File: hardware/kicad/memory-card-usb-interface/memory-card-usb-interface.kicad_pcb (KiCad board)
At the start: 2 copper layers, 16.6 x 40 mm, 9 parts, among them J1 USB_B, J2 DB9_Male, J3 CONN_MCU_VPP, J4 CONN_MCU_LOG, U1 PIC16F1454-IP

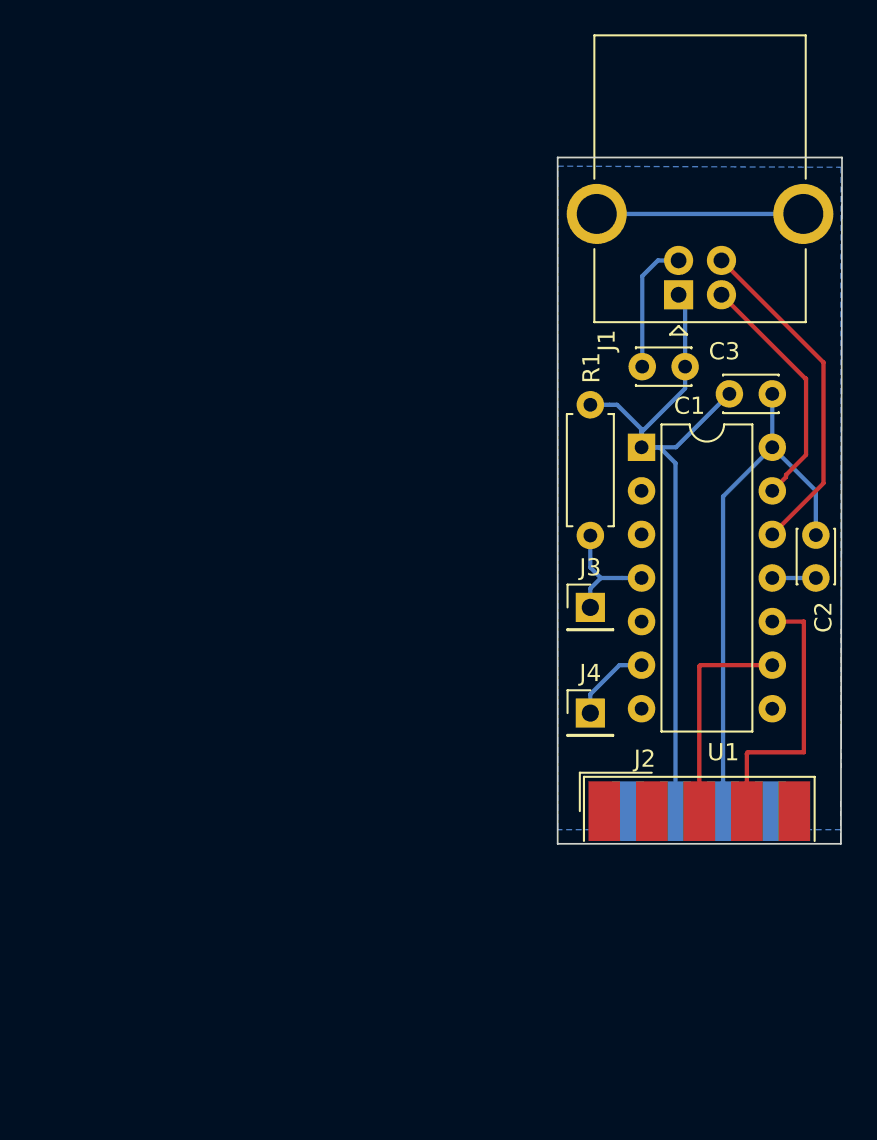
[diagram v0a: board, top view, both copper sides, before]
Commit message: Improvement to the schematic and PCB for available component dimensions and I2C pull-ups.
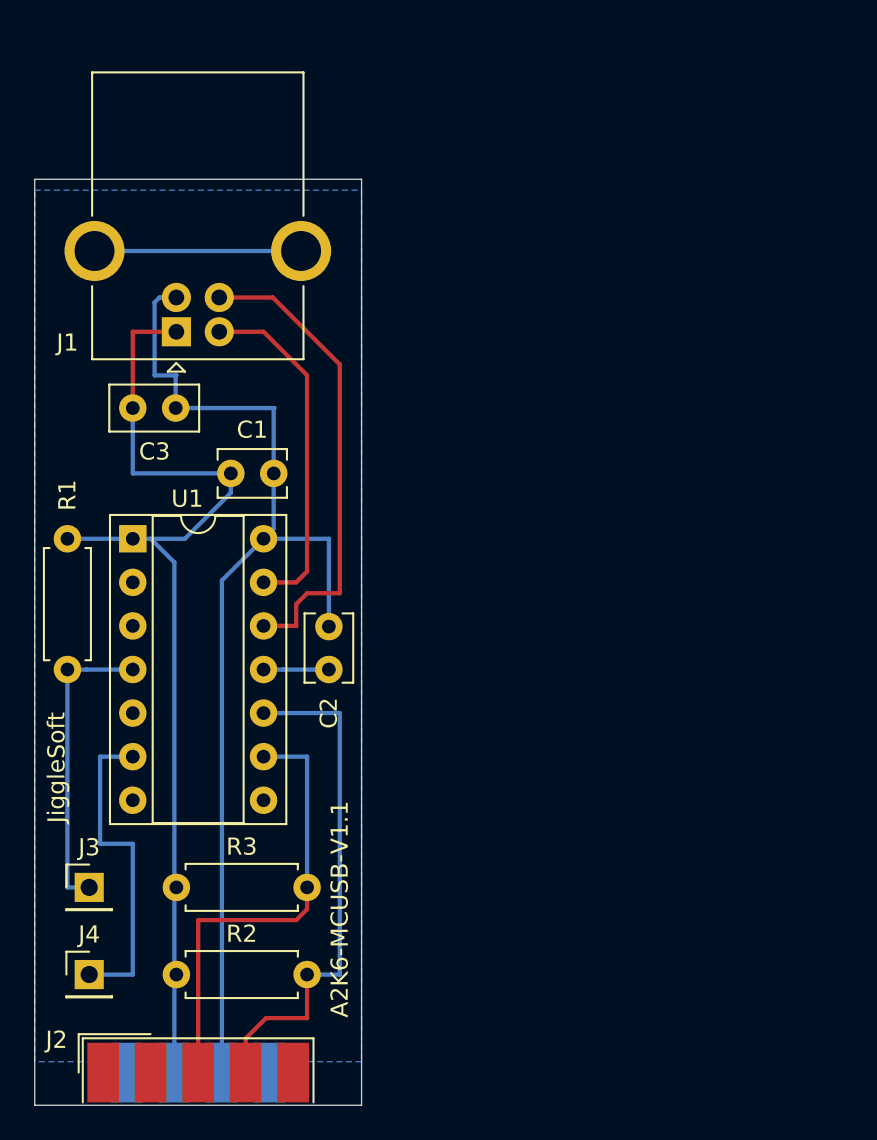
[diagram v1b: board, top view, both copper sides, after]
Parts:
- added R2: 10K, Resistor_THT:R_Axial_DIN0207_L6.3mm_D2.5mm_P7.62mm_Horizontal, F.Cu at (134.6, 128.9)
- added R3: 10K, Resistor_THT:R_Axial_DIN0207_L6.3mm_D2.5mm_P7.62mm_Horizontal, F.Cu at (134.6, 123.8)
- C1, C2: footprint Capacitor_THT:C_Disc_D3.0mm_W2.0mm_P2.50mm -> Capacitor_THT:C_Disc_D3.8mm_W2.6mm_P2.50mm
- C3: footprint Capacitor_THT:C_Disc_D3.0mm_W2.0mm_P2.50mm -> Capacitor_THT:C_Disc_D5.0mm_W2.5mm_P2.50mm
- U1: footprint Package_DIP:DIP-14_W7.62mm -> Package_DIP:DIP-14_W7.62mm_Socket
- moved J3 33.5 mm to (129.5, 123.8)
- moved J2 32.9 mm to (135.9, 134.6)
- moved J4 32.9 mm to (129.5, 128.9)
- moved C3 32.3 mm to (132.1, 95.9), turned to 0 degrees
- moved R1 31.5 mm to (128.3, 103.5)
- moved U1 30.1 mm to (132.1, 103.5)
- moved C1 29.4 mm to (137.8, 99.7)
- moved J1 29.4 mm to (134.6, 91.4)
- moved C2 28.9 mm to (143.5, 111.1)
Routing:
- net GNDPWR: track 39.5 -> 63.5 mm
- net /MCU_VDD: track 42.9 -> 60.0 mm
- net Net-(J4-Pad1): track 4.79 -> 19.1 mm
- net /MEM_SDA: track 12.7 -> 26.9 mm
- net /MEM_SCL: track 16.2 -> 30.2 mm
- net Net-(J3-Pad1): track 7.07 -> 17.8 mm
- net /USB_D-: track 19.7 -> 29.1 mm
- net /USB_D+: track 14.3 -> 20.4 mm
- net Net-(C2-Pad1): track 2.54 -> 3.81 mm
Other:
- board size 16.6 x 40 mm -> 19 x 54 mm
- board text added: "A2K6-MCUSB-V1.1"
- board text added: "JiggleSoft"
